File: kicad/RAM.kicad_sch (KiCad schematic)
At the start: 0 parts

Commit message: update schematic
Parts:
- added U8: AS6C62256-55SINTR, SOP-28_MIL330_ALL, symbol AS6C62256_55SIN:AS6C62256-55SINTR
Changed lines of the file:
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@@
 	(generator_version "9.0")
 	(paper "A4")
+	(symbol
+		(lib_id "AS6C62256_55SIN:AS6C62256-55SINTR")
+		(at 144.78 88.9 0)
+		(unit 1)
+		(exclude_from_sim no)
+		(in_bom yes)
+		(on_board yes)
+		(dnp no)
+		(fields_autoplaced yes)
+		(property "Reference" "U8"
+			(at 138.43 64.77 0)
+			(effects
+				(font
+					(size 1.524 1.524)
+				)
+			)
+		)
+		(property "Value" "AS6C62256-55SINTR"
+			(at 138.43 67.31 0)
+			(effects
+				(font
+					(size 1.524 1.524)
+				)
+			)
+		)
+		(property "Footprint" "SOP-28_MIL330_ALL"
+			(at 110.49 74.93 0)
+			(effects
+				(font
+					(size 1.27 1.27)
+					(italic yes)
+				)
+				(hide yes)
+			)
+		)
+		(property "Datasheet" "AS6C62256-55SINTR"
+			(at 110.49 74.93 0)
+			(effects
+				(font
+					(size 1.27 1.27)
+					(italic yes)
+				)
+				(hide yes)
+			)
+		)
+		(property "Description" ""
+			(at 144.78 88.9 0)
+			(effects
+				(font
+					(size 1.27 1.27)
+				)
+				(hide yes)
+			)
+		)
+		(pin "1"
+		)
+		(pin "3"
+		)
+		(pin "2"
+		)
+		(pin "5"
+		)
+		(pin "6"
+		)
+		(pin "7"
+		)
+		(pin "4"
+		)
+		(pin "8"
+		)
+		(pin "10"
+		)
+		(pin "12"
+		)
+		(pin "13"
+		)
+		(pin "14"
+		)
+		(pin "28"
+		)
+		(pin "26"
+		)
+		(pin "27"
+		)
+		(pin "11"
+		)
+		(pin "25"
+		)
+		(pin "24"
+		)
+		(pin "9"
+		)
+		(pin "19"
+		)
+		(pin "17"
+		)
+		(pin "21"
+		)
+		(pin "23"
+		)
+		(pin "22"
+		)
+		(pin "20"
+		)
+		(pin "18"
+		)
+		(pin "16"
+		)
+		(pin "15"
+		)
+		(instances
+			(project ""
+				(path "/d90612be-a4bb-4b59-8bc6-93e31ea1f515/c1016b1f-be48-40f8-9117-16b50a08909f"
+					(reference "U8")
+					(unit 1)
+				)
+			)
+		)
+	)
 )

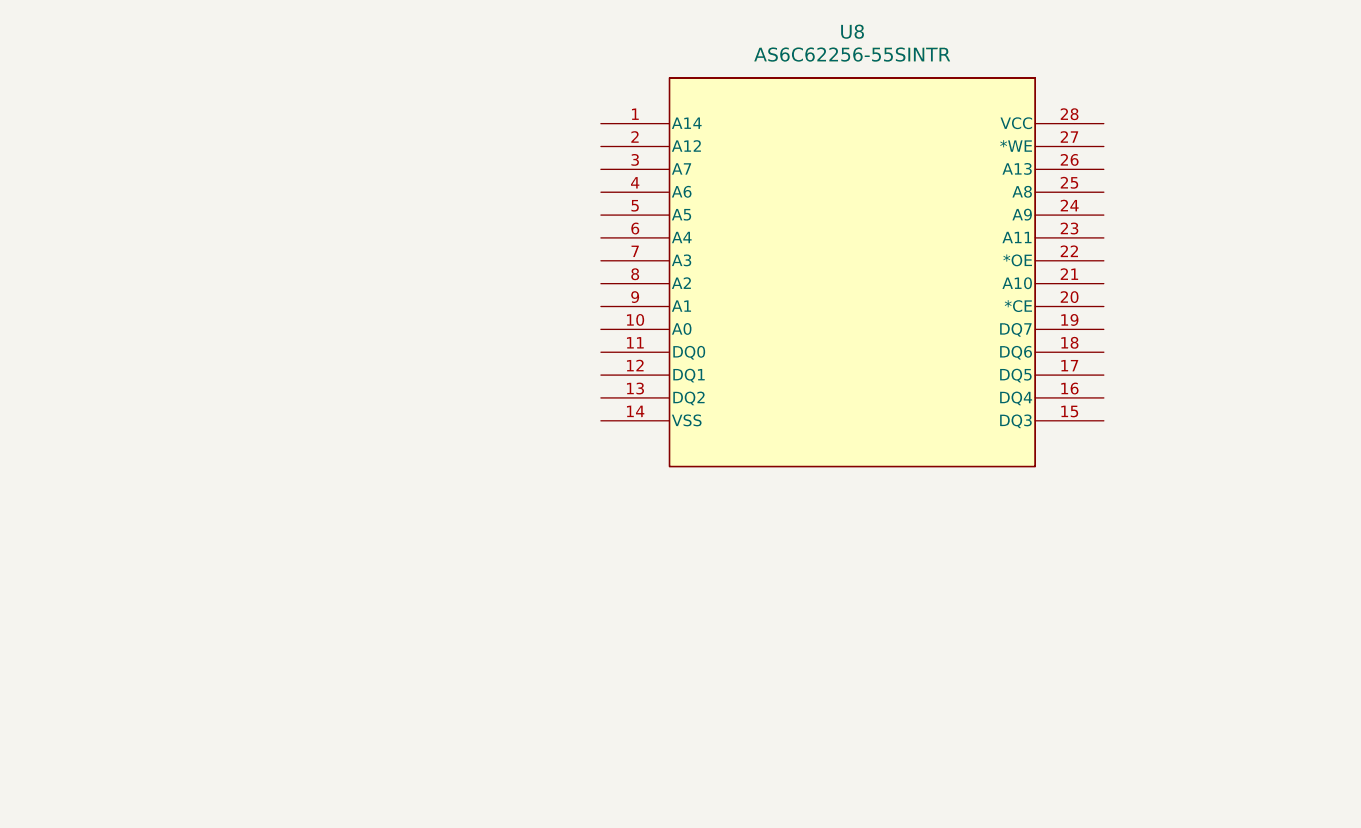
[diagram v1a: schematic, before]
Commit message: update schematic
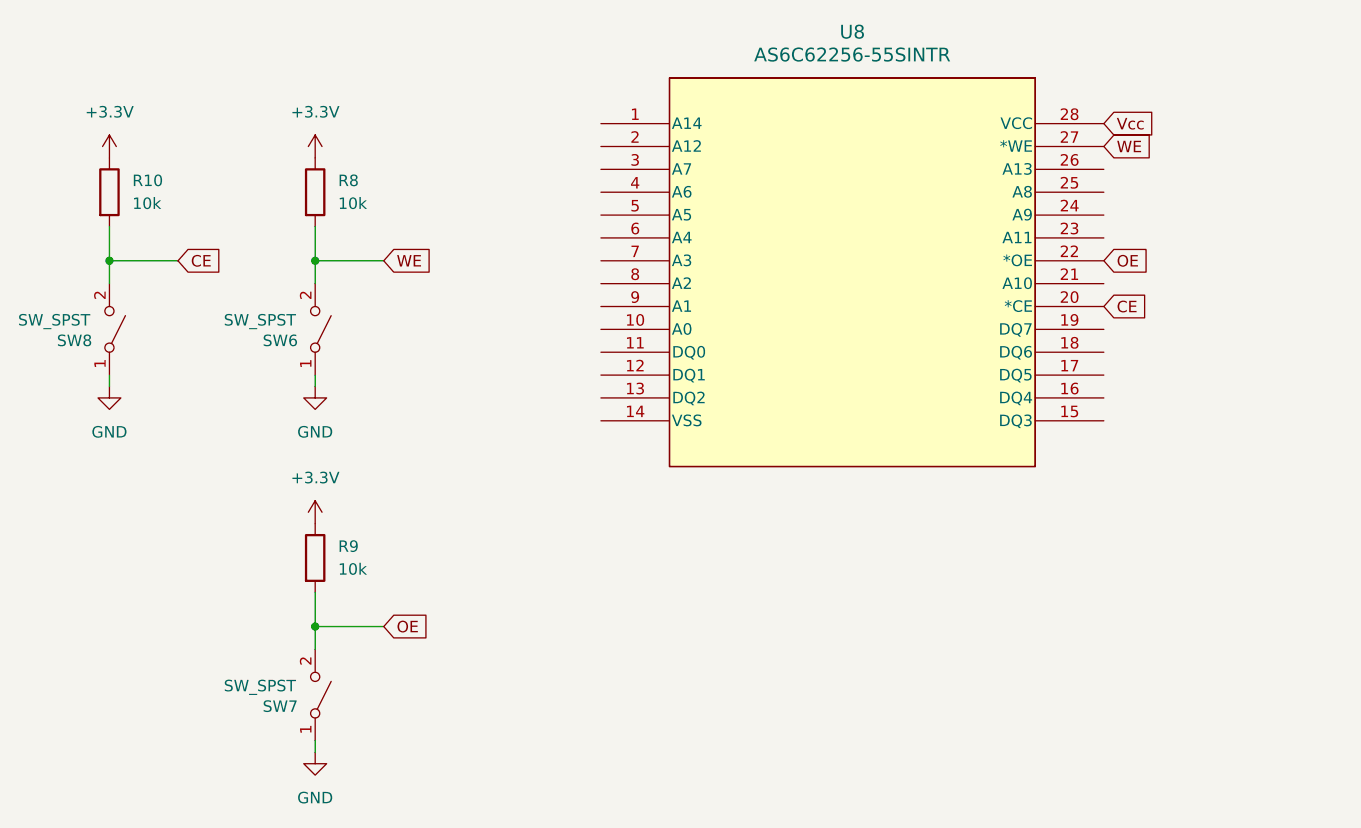
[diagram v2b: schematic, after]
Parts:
- added R10, R8, R9: 10k, symbol Device:R
- added SW6, SW7, SW8: SW_SPST, symbol Switch:SW_SPST
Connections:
- net CE: now reaches U8.20 (*CE)
- net CE: now also R10.2, SW8.2 (B)
- net OE: now reaches U8.22 (*OE)
- net OE: now also R9.2, SW7.2 (B)
- net WE: now reaches U8.27 (*WE)
- net WE: now also R8.2, SW6.2 (B)
- net Vcc: now reaches U8.28 (VCC)
- new net +3.3V: R10.1, R8.1, R9.1
- new net GND: SW6.1 (A), SW7.1 (A), SW8.1 (A)

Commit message: update schematic
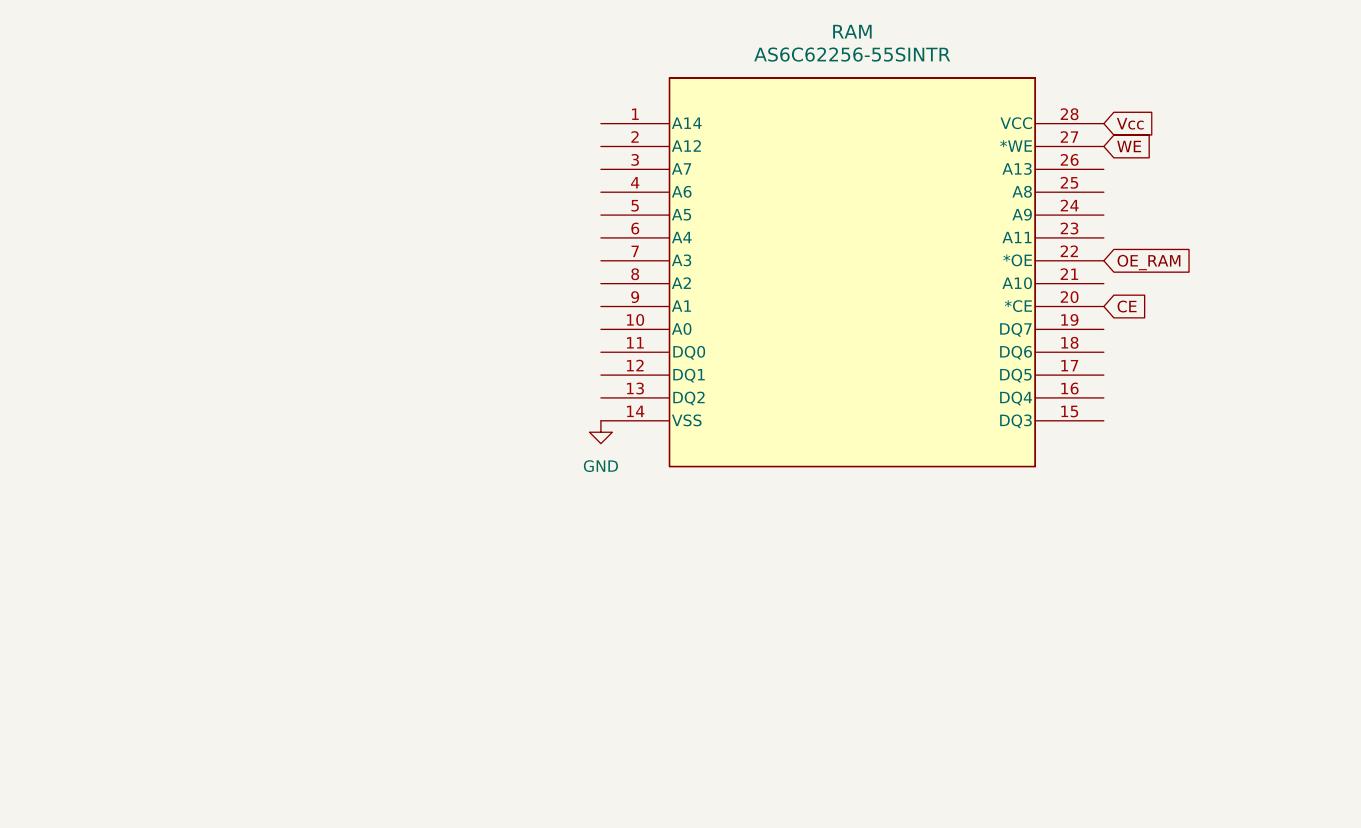
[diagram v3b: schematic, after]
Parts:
- removed R10, R8, R9: 10k, symbol Device:R
- removed SW6, SW7, SW8: SW_SPST, symbol Switch:SW_SPST
- renumbered U8 to RAM
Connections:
- net GND: now also RAM.14 (VSS)
- net OE renamed OE_RAM

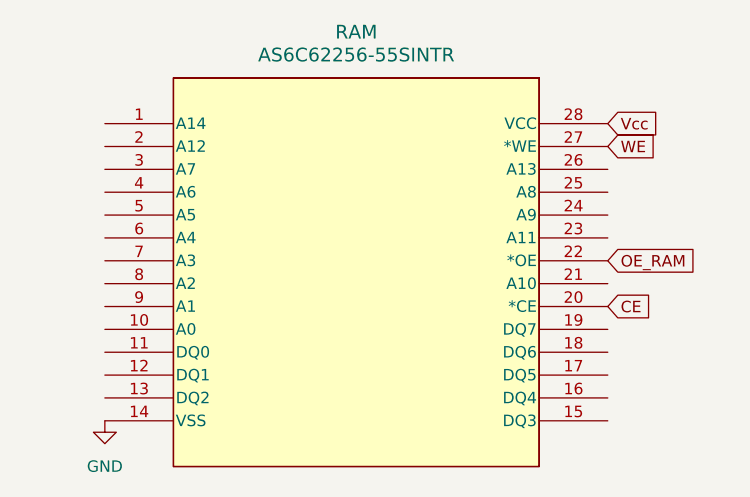
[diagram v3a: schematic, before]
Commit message: update schematic
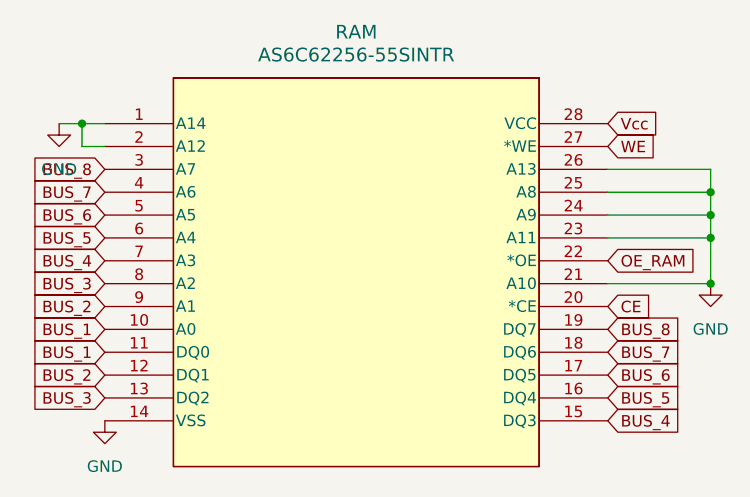
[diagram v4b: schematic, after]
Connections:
- net GND: now also RAM.1 (A14), RAM.2 (A12), RAM.21 (A10), RAM.23 (A11), RAM.24 (A9), RAM.25 (A8), RAM.26 (A13)
- net BUS_1: now reaches RAM.10 (A0)
- net BUS_1: now also RAM.11 (DQ0)
- net BUS_2: now reaches RAM.12 (DQ1)
- net BUS_2: now also RAM.9 (A1)
- net BUS_3: now reaches RAM.13 (DQ2)
- net BUS_3: now also RAM.8 (A2)
- net BUS_4: now reaches RAM.15 (DQ3)
- net BUS_4: now also RAM.7 (A3)
- net BUS_5: now reaches RAM.16 (DQ4)
- net BUS_5: now also RAM.6 (A4)
- net BUS_6: now reaches RAM.17 (DQ5)
- net BUS_6: now also RAM.5 (A5)
- net BUS_7: now reaches RAM.18 (DQ6)
- net BUS_7: now also RAM.4 (A6)
- net BUS_8: now reaches RAM.19 (DQ7)
- net BUS_8: now also RAM.3 (A7)

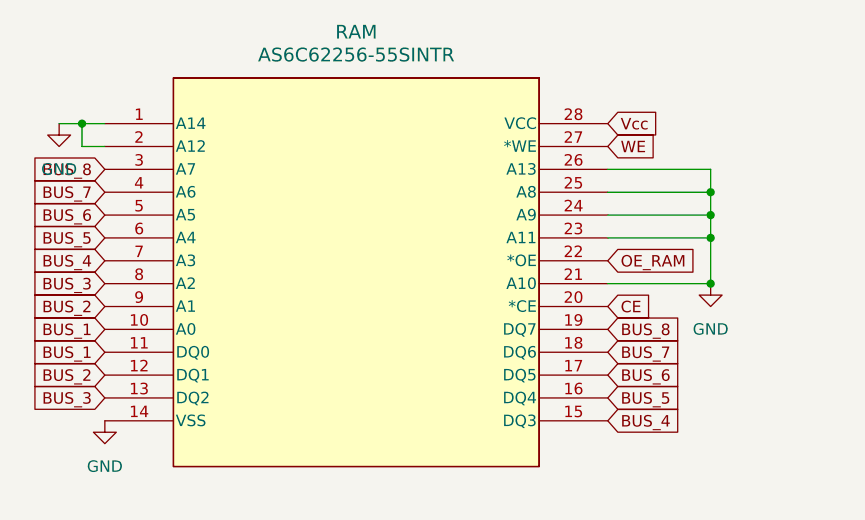
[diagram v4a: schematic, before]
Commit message: add PC
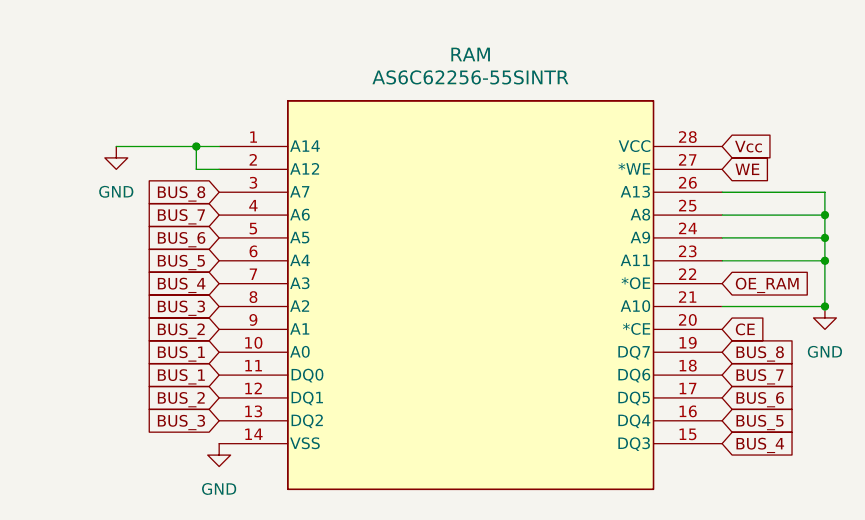
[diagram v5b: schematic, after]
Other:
- moved on the sheet: RAM
